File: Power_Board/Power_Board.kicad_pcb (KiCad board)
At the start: 2 copper layers, 47.8 x 64.3 mm, 20 parts, among them J1 Conn_01x10_Female, J2 Conn_01x10_Female, J3 Conn_01x06_Male, J4 Screw_Terminal_01x02, J5 Screw_Terminal_01x02

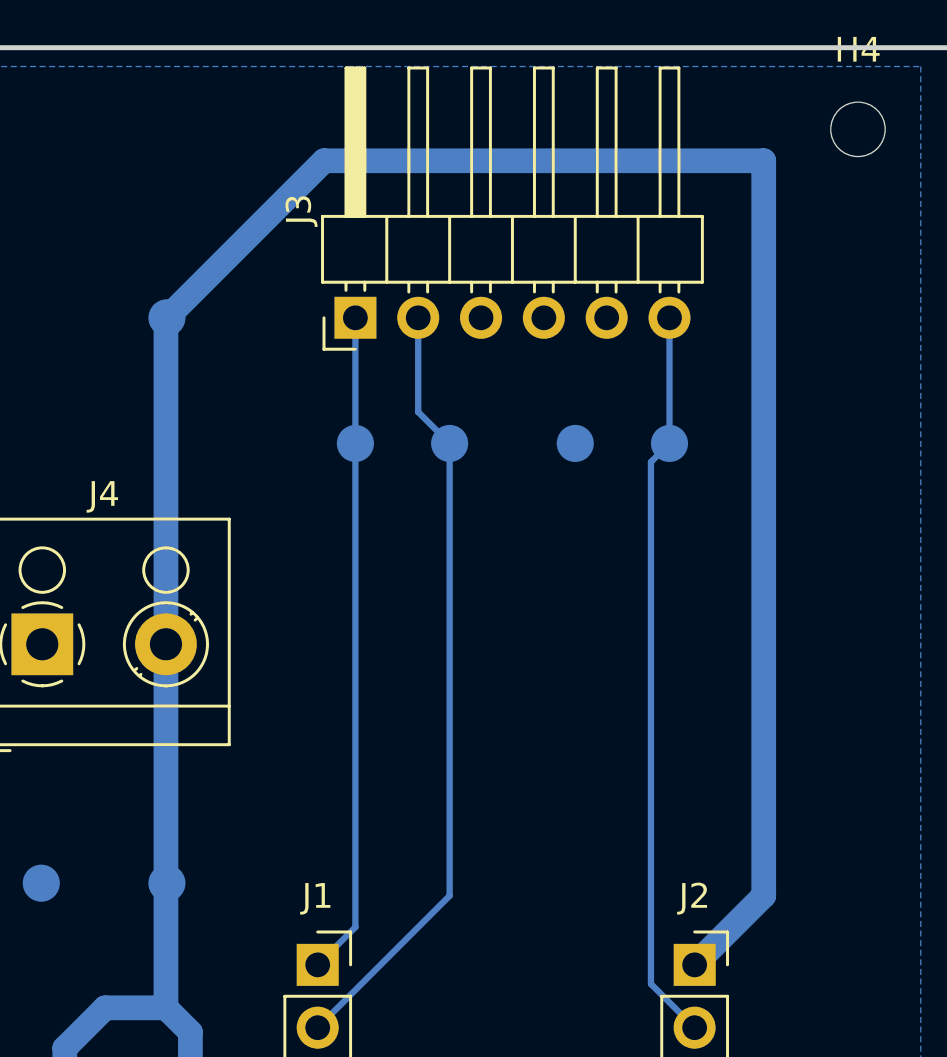
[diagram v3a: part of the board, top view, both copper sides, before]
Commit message: Added off switch(jumper)
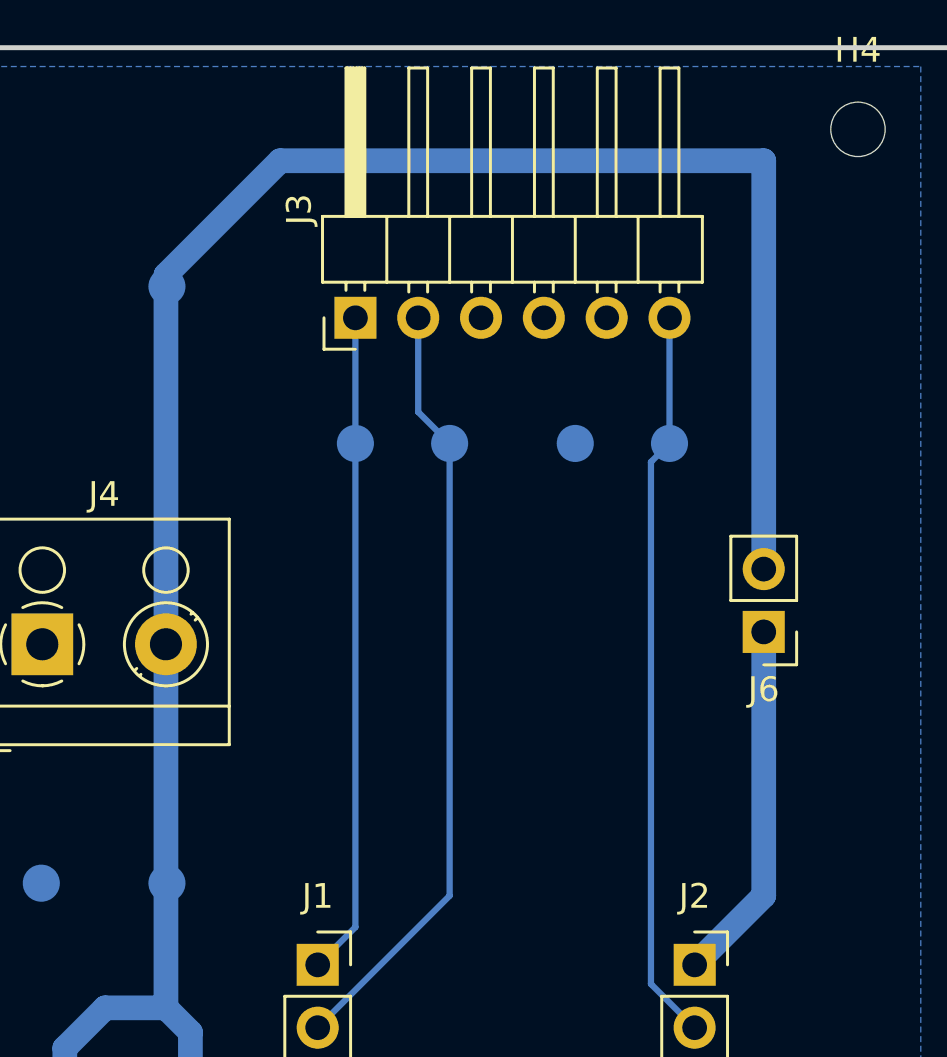
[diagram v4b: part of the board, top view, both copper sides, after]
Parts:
- added J6: Conn_01x02_Male, Connector_PinHeader_2.54mm:PinHeader_1x02_P2.54mm_Vertical, F.Cu at (162.6, 69.8)
- moved TP8 1.27 mm to (138.4, 55.9)
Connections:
- net VDDOUT renamed 3V3
- D1 pad 2: VBUS -> C+
- D2 pad 2: VBUS -> C+
- J4 pad 2: VBUS -> C+
- TP3 pad 1: VBUS -> C+
- TP8 pad 1: VBUS -> C+
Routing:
- net VBUS: track 102.8 -> 14.6 mm
- net C+: track 0.00 -> 86.7 mm
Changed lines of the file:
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@@
 (kicad_pcb (version 20211014) (generator pcbnew)
   (general
-    (thickness 1.6)
+    (thickness 1.64)
   )
   (paper "A4")
@@
       (layer "F.Mask" (type "Top Solder Mask") (thickness 0.01))
       (layer "F.Cu" (type "copper") (thickness 0.035))
-      (layer "dielectric 1" (type "core") (thickness 1.51) (material "FR4") (epsilon_r 4.5) (loss_tangent 0.02))
+      (layer "dielectric 1" (type "core") (thickness 1.55) (material "FR4") (epsilon_r 4.5) (loss_tangent 0.02))
       (layer "B.Cu" (type "copper") (thickness 0.035))
       (layer "B.Mask" (type "Bottom Solder Mask") (thickness 0.01))
@@
   (net 20 "INT")
   (net 21 "1V8")
-  (net 22 "VDDOUT")
+  (net 22 "C+")
+  (net 23 "3V3")
   (footprint "Connector_PinSocket_2.54mm:PinSocket_1x10_P2.54mm_Vertical" (layer "F.Cu")
     (at 144.526 83.312)
@@
       (net 1 "GND") (pinfunction "Pin_5") (pintype "passive"))
     (pad "6" thru_hole oval (at 0 12.7 90) (size 1.7 1.7) (drill 1) (layers *.Cu *.Mask)
-      (net 22 "VDDOUT") (pinfunction "Pin_6") (pintype "passive"))
+      (net 23 "3V3") (pinfunction "Pin_6") (pintype "passive"))
     (model "${KICAD6_3DMODEL_DIR}/Connector_PinHeader_2.54mm.3dshapes/PinHeader_1x06_P2.54mm_Horizontal.wrl"
       (offset (xyz 0 0 0))
@@
       (net 2 "VBUS") (pinfunction "Pin_1") (pintype "passive"))
     (pad "2" thru_hole oval (at 0 2.54) (size 1.7 1.7) (drill 1) (layers *.Cu *.Mask)
-      (net 22 "VDDOUT") (pinfunction "Pin_2") (pintype "passive"))
+      (net 23 "3V3") (pinfunction "Pin_2") (pintype "passive"))
     (pad "3" thru_hole oval (at 0 5.08) (size 1.7 1.7) (drill 1) (layers *.Cu *.Mask)
       (net 1 "GND") (pinfunction "Pin_3") (pintype "passive"))
@@
       (net 1 "GND") (pinfunction "Pin_1") (pintype "passive"))
     (pad "2" thru_hole circle (at 5 0) (size 2.5 2.5) (drill 1.3) (layers *.Cu *.Mask)
-      (net 2 "VBUS") (pinfunction "Pin_2") (pintype "passive"))
+      (net 22 "C+") (pinfunction "Pin_2") (pintype "passive"))
     (model "${KICAD6_3DMODEL_DIR}/TerminalBlock_RND.3dshapes/TerminalBlock_RND_205-00001_1x02_P5.00mm_Horizontal.wrl"
+      (offset (xyz 0 0 0))
+      (scale (xyz 1 1 1))
+      (rotate (xyz 0 0 0))
+    )
+  )
+  (footprint "Connector_PinHeader_2.54mm:PinHeader_1x02_P2.54mm_Vertical" (layer "F.Cu")
+    (at 162.56 69.85 180)
+    (descr "Through hole straight pin header, 1x02, 2.54mm pitch, single row")
+    (tags "Through hole pin header THT 1x02 2.54mm single row")
+    (property "Sheetfile" "Power_Board.kicad_sch")
+    (property "Sheetname" "")
+    (attr through_hole)
+    (fp_text reference "J6" (at 0 -2.33) (layer "F.SilkS")
+      (effects (font (size 1 1) (thickness 0.15)))
+    )
+    (fp_text value "Conn_01x02_Male" (at 0 4.87) (layer "F.Fab")
+      (effects (font (size 1 1) (thickness 0.15)))
+    )
+    (fp_text user "${REFERENCE}" (at 0 1.27 90) (layer "F.Fab")
+      (effects (font (size 1 1) (thickness 0.15)))
+    )
+    (fp_line (start 1.33 1.27) (end 1.33 3.87) (layer "F.SilkS") (width 0.12))
+    (fp_line (start -1.33 -1.33) (end 0 -1.33) (layer "F.SilkS") (width 0.12))
+    (fp_line (start -1.33 0) (end -1.33 -1.33) (layer "F.SilkS") (width 0.12))
+    (fp_line (start -1.33 3.87) (end 1.33 3.87) (layer "F.SilkS") (width 0.12))
+    (fp_line (start -1.33 1.27) (end 1.33 1.27) (layer "F.SilkS") (width 0.12))
+    (fp_line (start -1.33 1.27) (end -1.33 3.87) (layer "F.SilkS") (width 0.12))
+    (fp_line (start 1.8 -1.8) (end -1.8 -1.8) (layer "F.CrtYd") (width 0.05))
+    (fp_line (start -1.8 -1.8) (end -1.8 4.35) (layer "F.CrtYd") (width 0.05))
+    (fp_line (start 1.8 4.35) (end 1.8 -1.8) (layer "F.CrtYd") (width 0.05))
+    (fp_line (start -1.8 4.35) (end 1.8 4.35) (layer "F.CrtYd") (width 0.05))
+    (fp_line (start 1.27 -1.27) (end 1.27 3.81) (layer "F.Fab") (width 0.1))
+    (fp_line (start 1.27 3.81) (end -1.27 3.81) (layer "F.Fab") (width 0.1))
+    (fp_line (start -1.27 3.81) (end -1.27 -0.635) (layer "F.Fab") (width 0.1))
+    (fp_line (start -1.27 -0.635) (end -0.635 -1.27) (layer "F.Fab") (width 0.1))
+    (fp_line (start -0.635 -1.27) (end 1.27 -1.27) (layer "F.Fab") (width 0.1))
+    (pad "1" thru_hole rect (at 0 0 180) (size 1.7 1.7) (drill 1) (layers *.Cu *.Mask)
+      (net 2 "VBUS") (pinfunction "Pin_1") (pintype "passive"))
+    (pad "2" thru_hole oval (at 0 2.54 180) (size 1.7 1.7) (drill 1) (layers *.Cu *.Mask)
+      (net 22 "C+") (pinfunction "Pin_2") (pintype "passive"))
+    (model "${KICAD6_3DMODEL_DIR}/Connector_PinHeader_2.54mm.3dshapes/PinHeader_1x02_P2.54mm_Vertical.wrl"
       (offset (xyz 0 0 0))
       (scale (xyz 1 1 1))
@@
       (net 1 "GND") (pintype "passive"))
     (pad "2" smd roundrect (at -0.9375 -0.95 270) (size 1.475 0.6) (layers "B.Cu" "B.Paste" "B.Mask") (roundrect_rratio 0.25)
-      (net 2 "VBUS") (pintype "passive"))
+      (net 22 "C+") (pintype "passive"))
     (pad "3" smd roundrect (at 0.9375 0 270) (size 1.475 0.6) (layers "B.Cu" "B.Paste" "B.Mask") (roundrect_rratio 0.25)
       (net 4 "Net-(D2-Pad3)") (pintype "passive"))
@@
     (fp_circle (center 0 0) (end 1.25 0) (layer "B.CrtYd") (width 0.05) (fill none))
     (pad "1" smd circle (at 0 0 180) (size 1.5 1.5) (layers "B.Cu" "B.Mask")
-      (net 22 "VDDOUT") (pinfunction "1") (pintype "passive"))
+      (net 23 "3V3") (pinfunction "1") (pintype "passive"))
   )
   (footprint "TestPoint:TestPoint_Pad_D1.5mm" (layer "B.Cu")
@@
     (fp_circle (center 0 0) (end 1.25 0) (layer "B.CrtYd") (width 0.05) (fill none))
     (pad "1" smd circle (at 0 0 180) (size 1.5 1.5) (layers "B.Cu" "B.Mask")
-      (net 2 "VBUS") (pinfunction "1") (pintype "passive"))
+      (net 22 "C+") (pinfunction "1") (pintype "passive"))
   )
   (footprint "TestPoint:TestPoint_Pad_D1.5mm" (layer "B.Cu")
@@
       (net 1 "GND") (pintype "passive"))
     (pad "2" smd roundrect (at -0.9375 -0.95 270) (size 1.475 0.6) (layers "B.Cu" "B.Paste" "B.Mask") (roundrect_rratio 0.25)
-      (net 2 "VBUS") (pintype "passive"))
+      (net 22 "C+") (pintype "passive"))
     (pad "3" smd roundrect (at 0.9375 0 270) (size 1.475 0.6) (layers "B.Cu" "B.Paste" "B.Mask") (roundrect_rratio 0.25)
       (net 3 "Net-(D1-Pad3)") (pintype "passive"))
@@
   )
   (footprint "TestPoint:TestPoint_Pad_D1.5mm" (layer "B.Cu")
-    (at 138.43 57.15 90)
+    (at 138.43 55.88 90)
     (descr "SMD pad as test Point, diameter 1.5mm")
     (tags "test point SMD pad")
@@
     (fp_circle (center 0 0) (end 1.25 0) (layer "B.CrtYd") (width 0.05) (fill none))
     (pad "1" smd circle (at 0 0 90) (size 1.5 1.5) (layers "B.Cu" "B.Mask")
-      (net 2 "VBUS") (pinfunction "1") (pintype "passive"))
+      (net 22 "C+") (pinfunction "1") (pintype "passive"))
   )
   (gr_rect (start 122.428 46.228) (end 170.18 110.49) (layer "Edge.Cuts") (width 0.2) (fill none))
   (gr_rect (start 159.512 111.572) (end 144.272 65.532) (layer "User.1") (width 0.15) (fill none))
-  (segment (start 135.93 85.05) (end 138.39 85.05) (width 1) (layer "B.Cu") (net 2))
-  (segment (start 134.3 86.68) (end 135.93 85.05) (width 1) (layer "B.Cu") (net 2))
-  (segment (start 139.38 86.04) (end 138.39 85.05) (width 1) (layer "B.Cu") (net 2))
-  (segment (start 139.38 90.5025) (end 139.38 86.04) (width 1) (layer "B.Cu") (net 2))
-  (segment (start 144.78 50.8) (end 162.56 50.8) (width 1) (layer "B.Cu") (net 2))
-  (segment (start 134.3 90.5025) (end 134.3 86.68) (width 1) (layer "B.Cu") (net 2))
-  (segment (start 162.56 50.8) (end 162.56 80.518) (width 1) (layer "B.Cu") (net 2))
-  (segment (start 138.39 57.19) (end 144.78 50.8) (width 1) (layer "B.Cu") (net 2))
   (segment (start 162.56 80.518) (end 159.766 83.312) (width 1) (layer "B.Cu") (net 2))
-  (segment (start 138.39 70.35) (end 138.39 57.19) (width 1) (layer "B.Cu") (net 2))
-  (segment (start 138.39 85.05) (end 138.39 70.35) (width 1) (layer "B.Cu") (net 2))
+  (segment (start 162.56 69.85) (end 162.56 80.518) (width 1) (layer "B.Cu") (net 2))
   (segment (start 133.39 102.37) (end 133.39 92.4175) (width 1) (layer "B.Cu") (net 3))
   (segment (start 133.39 92.4175) (end 133.35 92.3775) (width 0.254) (layer "B.Cu") (net 3))
@@
   (segment (start 148.59 60.96) (end 149.86 62.23) (width 0.254) (layer "B.Cu") (net 6))
   (segment (start 144.526 85.852) (end 149.86 80.518) (width 0.254) (layer "B.Cu") (net 6))
-  (segment (start 158 84.086) (end 159.766 85.852) (width 0.254) (layer "B.Cu") (net 22))
-  (segment (start 158 62.98) (end 158 84.086) (width 0.254) (layer "B.Cu") (net 22))
-  (segment (start 158.75 62.23) (end 158.75 57.15) (width 0.254) (layer "B.Cu") (net 22))
-  (segment (start 158.75 62.23) (end 158 62.98) (width 0.254) (layer "B.Cu") (net 22))
+  (segment (start 138.39 70.35) (end 138.39 55.416576) (width 1) (layer "B.Cu") (net 22))
+  (segment (start 135.93 85.05) (end 138.39 85.05) (width 1) (layer "B.Cu") (net 22))
+  (segment (start 134.3 86.68) (end 135.93 85.05) (width 1) (layer "B.Cu") (net 22))
+  (segment (start 143.006576 50.8) (end 162.56 50.8) (width 1) (layer "B.Cu") (net 22))
+  (segment (start 139.38 86.04) (end 138.39 85.05) (width 1) (layer "B.Cu") (net 22))
+  (segment (start 139.38 90.5025) (end 139.38 86.04) (width 1) (layer "B.Cu") (net 22))
+  (segment (start 162.56 50.8) (end 162.56 67.31) (width 1) (layer "B.Cu") (net 22))
+  (segment (start 134.3 90.5025) (end 134.3 86.68) (width 1) (layer "B.Cu") (net 22))
+  (segment (start 138.39 55.416576) (end 143.006576 50.8) (width 1) (layer "B.Cu") (net 22))
+  (segment (start 138.39 85.05) (end 138.39 70.35) (width 1) (layer "B.Cu") (net 22))
+  (segment (start 158 84.086) (end 159.766 85.852) (width 0.254) (layer "B.Cu") (net 23))
+  (segment (start 158 62.98) (end 158 84.086) (width 0.254) (layer "B.Cu") (net 23))
+  (segment (start 158.75 62.23) (end 158.75 57.15) (width 0.254) (layer "B.Cu") (net 23))
+  (segment (start 158.75 62.23) (end 158 62.98) (width 0.254) (layer "B.Cu") (net 23))
   (zone (net 1) (net_name "GND") (layer "B.Cu") (hatch edge 0.508)
     (connect_pads (clearance 0.508))
